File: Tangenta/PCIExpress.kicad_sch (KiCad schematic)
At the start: 0 parts

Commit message: ...
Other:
- sheet PCIE_Slot_1 ports: added 12V, PCIE1_nWAKE; removed none
- sheet PCIE_Slot_2 ports: added 12V, PCIE2_nWAKE; removed none
- sheet PCIE_Slot_3 ports: added 12V, PCIE3_nWAKE; removed none
- note removed: "Do not forget 12V"
- note removed: "Guide the nWAKE through all slots use 0R to optionally disconnect"
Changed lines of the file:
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@@
 (kicad_sch (version 20230121) (generator eeschema)
   (paper "A3")
+  (junction (at 234.95 95.885) (diameter 0) (color 0 0 0 0)
+  )
+  (junction (at 226.06 117.475) (diameter 0) (color 0 0 0 0)
+  )
+  (junction (at 226.06 69.215) (diameter 0) (color 0 0 0 0)
+  )
+  (junction (at 234.95 144.145) (diameter 0) (color 0 0 0 0)
+  )
   (bus_entry (at 64.135 165.735) (size 2.54 -2.54)
     (stroke (width 0) (type default))
@@
     (stroke (width 0) (type default))
   )
+  (wire (pts (xy 226.06 117.475) (xy 226.06 168.275))
+    (stroke (width 0) (type default))
+  )
   (wire (pts (xy 176.53 175.26) (xy 187.96 175.26))
     (stroke (width 0) (type default))
@@
     (stroke (width 0) (type default))
   )
+  (wire (pts (xy 215.9 144.145) (xy 234.95 144.145))
+    (stroke (width 0) (type default))
+  )
   (wire (pts (xy 101.6 120.015) (xy 124.46 120.015))
     (stroke (width 0) (type default))
@@
     (stroke (width 0) (type default))
   )
+  (wire (pts (xy 101.6 46.99) (xy 234.95 46.99))
+    (stroke (width 0) (type default))
+  )
   (wire (pts (xy 101.6 147.955) (xy 124.46 147.955))
     (stroke (width 0) (type default))
   )
+  (wire (pts (xy 226.06 69.215) (xy 215.9 69.215))
+    (stroke (width 0) (type default))
+  )
   (wire (pts (xy 176.53 140.97) (xy 187.96 140.97))
     (stroke (width 0) (type default))
@@
     (stroke (width 0) (type default))
   )
+  (wire (pts (xy 234.95 95.885) (xy 234.95 144.145))
+    (stroke (width 0) (type default))
+  )
   (wire (pts (xy 176.53 194.31) (xy 187.96 194.31))
     (stroke (width 0) (type default))
@@
     (stroke (width 0) (type default))
   )
+  (wire (pts (xy 234.95 46.99) (xy 234.95 95.885))
+    (stroke (width 0) (type default))
+  )
   (wire (pts (xy 101.6 132.08) (xy 124.46 132.08))
     (stroke (width 0) (type default))
@@
     (stroke (width 0) (type default))
   )
+  (wire (pts (xy 226.06 55.245) (xy 226.06 69.215))
+    (stroke (width 0) (type default))
+  )
+  (wire (pts (xy 215.9 95.885) (xy 234.95 95.885))
+    (stroke (width 0) (type default))
+  )
   (wire (pts (xy 176.53 92.71) (xy 187.96 92.71))
     (stroke (width 0) (type default))
@@
     (stroke (width 0) (type default))
   )
+  (wire (pts (xy 101.6 55.245) (xy 226.06 55.245))
+    (stroke (width 0) (type default))
+  )
   (bus (pts (xy 64.135 110.49) (xy 64.135 113.665))
     (stroke (width 0) (type default))
@@
     (stroke (width 0) (type default))
   )
+  (wire (pts (xy 234.95 194.945) (xy 215.9 194.945))
+    (stroke (width 0) (type default))
+  )
   (bus (pts (xy 64.135 120.015) (xy 64.135 126.365))
     (stroke (width 0) (type default))
@@
     (stroke (width 0) (type default))
   )
+  (wire (pts (xy 234.95 144.145) (xy 234.95 194.945))
+    (stroke (width 0) (type default))
+  )
   (wire (pts (xy 101.6 122.555) (xy 124.46 122.555))
     (stroke (width 0) (type default))
@@
     (stroke (width 0) (type default))
   )
+  (wire (pts (xy 226.06 69.215) (xy 226.06 117.475))
+    (stroke (width 0) (type default))
+  )
   (wire (pts (xy 66.675 172.72) (xy 85.09 172.72))
     (stroke (width 0) (type default))
@@
     (stroke (width 0) (type default))
   )
+  (wire (pts (xy 226.06 168.275) (xy 215.9 168.275))
+    (stroke (width 0) (type default))
+  )
   (wire (pts (xy 66.675 90.17) (xy 81.915 90.17))
     (stroke (width 0) (type default))
   )
+  (wire (pts (xy 226.06 117.475) (xy 215.9 117.475))
+    (stroke (width 0) (type default))
+  )
   (wire (pts (xy 176.53 135.89) (xy 187.96 135.89))
     (stroke (width 0) (type default))
@@
     (stroke (width 0) (type default))
   )
-  (text "Guide the nWAKE through all slots\nuse 0R to optionally disconnect"
-    (at 256.54 162.56 0)
-    (effects (font (size 5 5)) (justify left bottom))
-  )
-  (text "Do not forget 12V" (at 256.54 109.22 0)
-    (effects (font (size 5 5)) (justify left bottom))
-  )
   (label "PCIE_X1_CLK.P" (at 81.915 90.17 180) (fields_autoplaced)
     (effects (font (size 1.27 1.27)) (justify right bottom))
@@
     (effects (font (size 1.27 1.27)) (justify left bottom))
   )
+  (label "12V" (at 124.46 46.99 180) (fields_autoplaced)
+    (effects (font (size 1.27 1.27)) (justify right bottom))
+  )
+  (label "PCIE_X1_CTRL.nWAKE" (at 101.6 55.245 0) (fields_autoplaced)
+    (effects (font (size 1.27 1.27)) (justify left bottom))
+  )
   (label "PCIE_X1_DATA.RX_P" (at 101.6 117.475 0) (fields_autoplaced)
     (effects (font (size 1.27 1.27)) (justify left bottom))
@@
   )
   (hierarchical_label "PCIE_X1_JTAG{TCK TDI TDO TMS TRST}" (shape input) (at 57.785 178.435 180) (fields_autoplaced)
+    (effects (font (size 1.27 1.27)) (justify right))
+  )
+  (hierarchical_label "12V" (shape input) (at 101.6 46.99 180) (fields_autoplaced)
     (effects (font (size 1.27 1.27)) (justify right))
   )
@@
       (effects (font (size 1.27 1.27)) (justify left))
     )
+    (pin "PCIE1_nWAKE" input (at 215.9 69.215 0)
+      (effects (font (size 1.27 1.27)) (justify right))
+    )
+    (pin "12V" input (at 215.9 95.885 0)
+      (effects (font (size 1.27 1.27)) (justify right))
+    )
     (instances
       (project "Tangenta"
@@
       (effects (font (size 1.27 1.27)) (justify left))
     )
+    (pin "PCIE2_nWAKE" input (at 215.9 117.475 0)
+      (effects (font (size 1.27 1.27)) (justify right))
+    )
+    (pin "12V" input (at 215.9 144.145 0)
+      (effects (font (size 1.27 1.27)) (justify right))
+    )
     (instances
       (project "Tangenta"
@@
       (effects (font (size 1.27 1.27)) (justify left))
     )
+    (pin "PCIE3_nWAKE" input (at 215.9 168.275 0)
+      (effects (font (size 1.27 1.27)) (justify right))
+    )
+    (pin "12V" input (at 215.9 194.945 0)
+      (effects (font (size 1.27 1.27)) (justify right))
+    )
     (instances

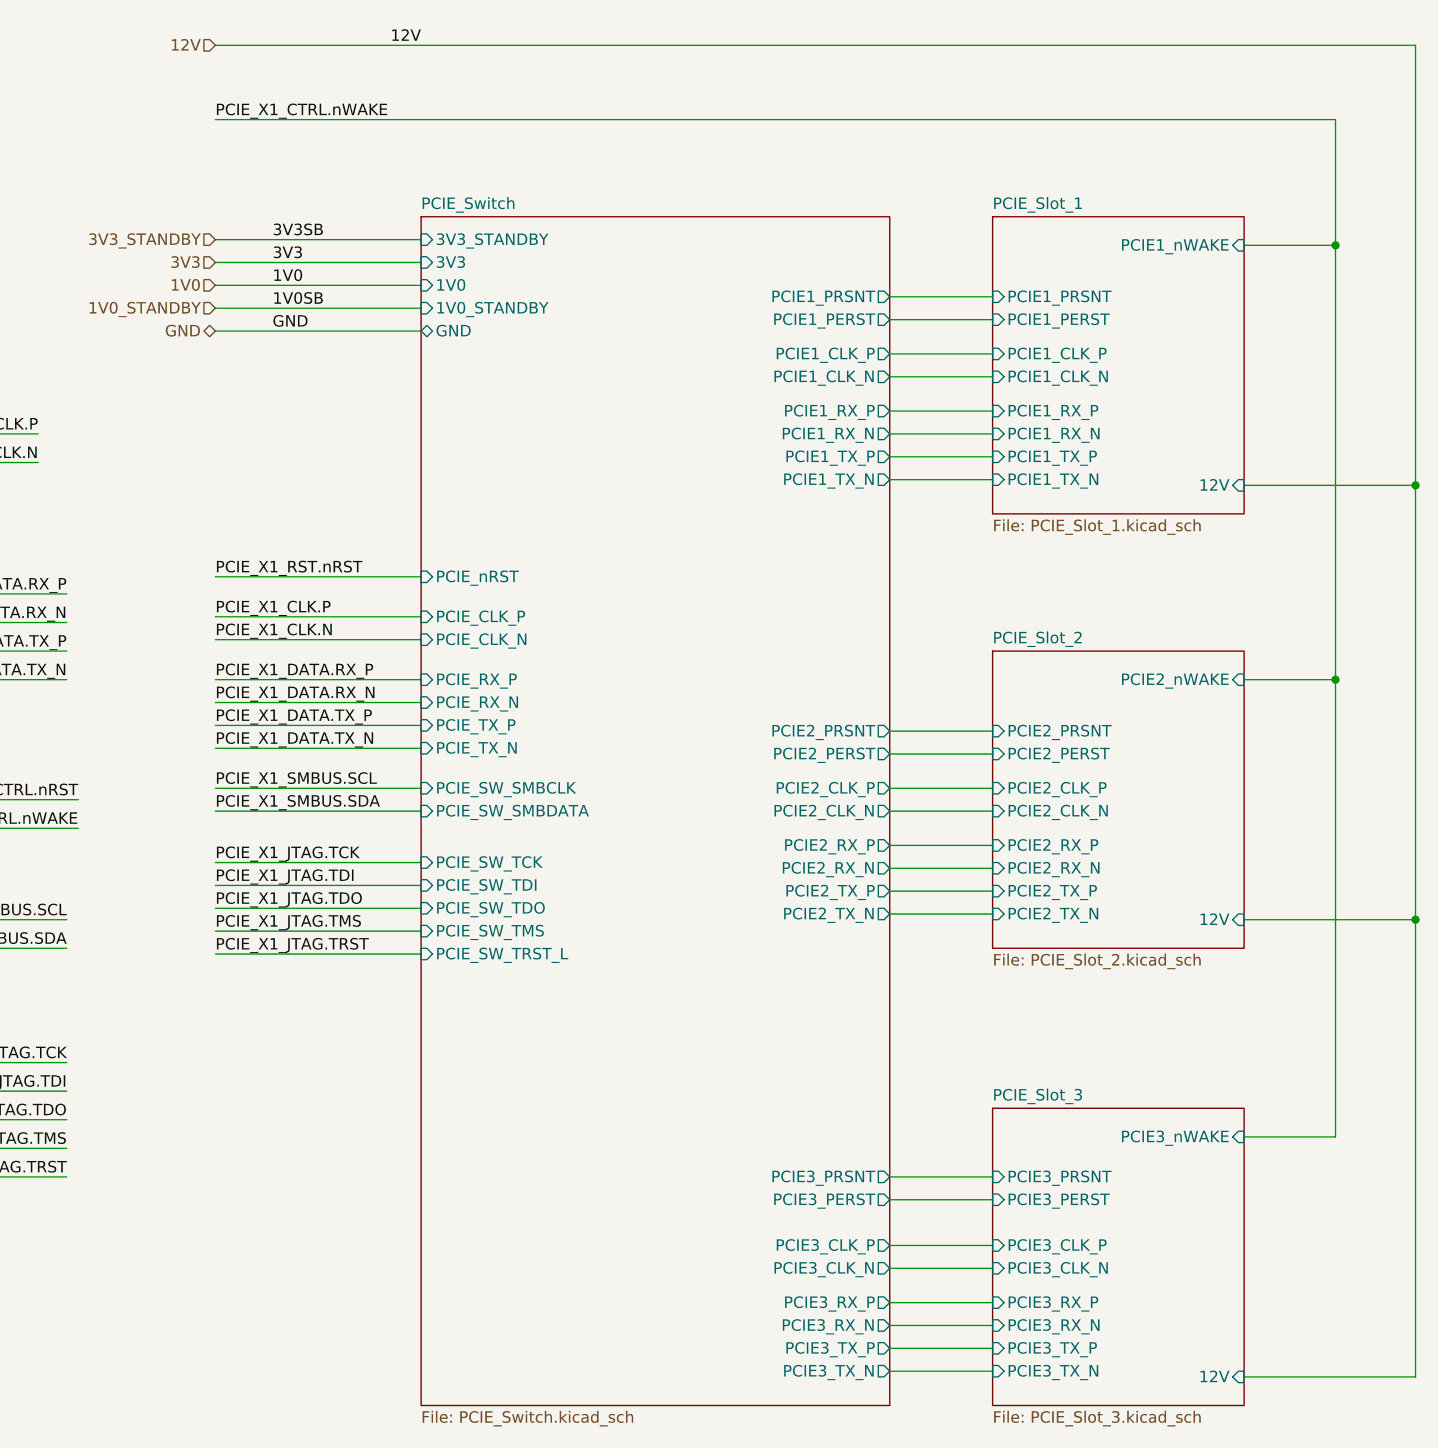
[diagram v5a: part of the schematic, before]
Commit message: PCIe switch schematic, continued...
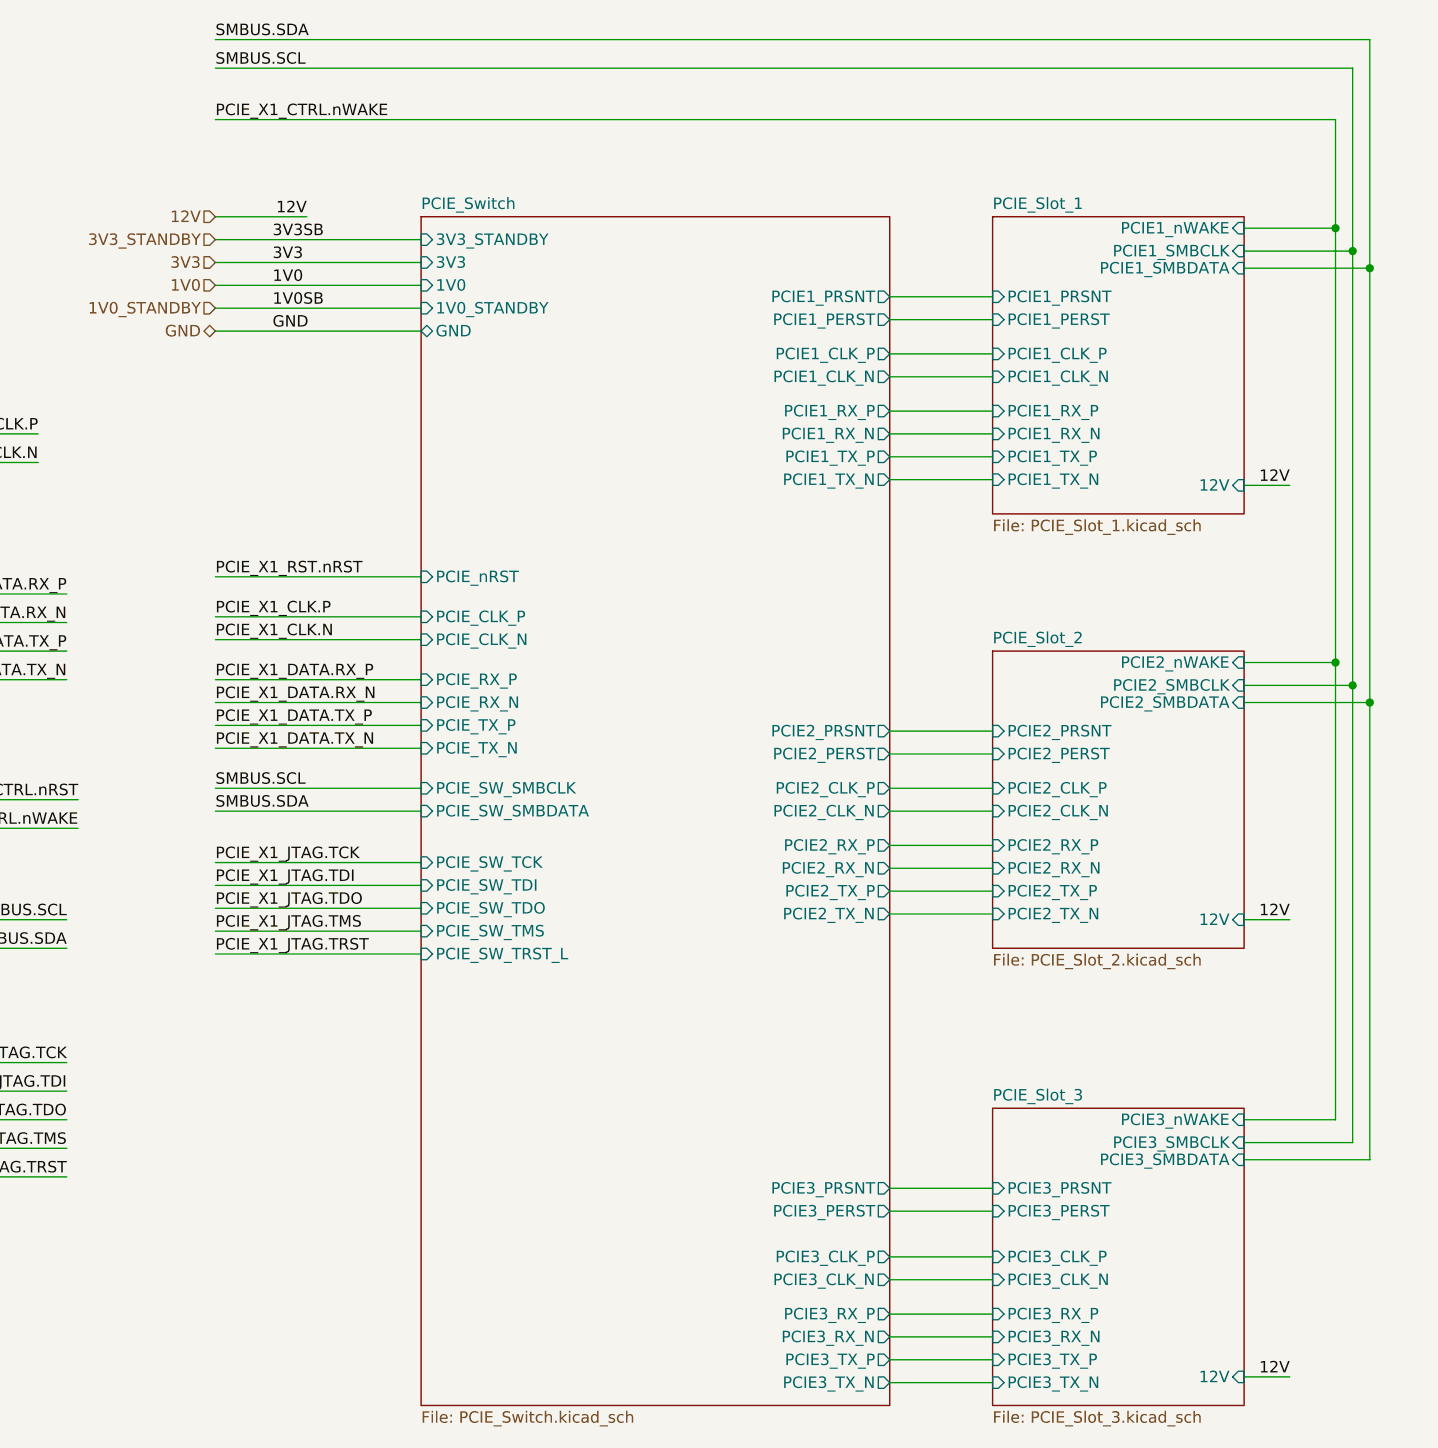
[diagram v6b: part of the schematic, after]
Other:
- sheet PCIE_Slot_1 ports: added PCIE1_SMBCLK, PCIE1_SMBDATA; removed none
- sheet PCIE_Slot_2 ports: added PCIE2_SMBCLK, PCIE2_SMBDATA; removed none
- sheet PCIE_Slot_3 ports: added PCIE3_SMBCLK, PCIE3_SMBDATA; removed none
